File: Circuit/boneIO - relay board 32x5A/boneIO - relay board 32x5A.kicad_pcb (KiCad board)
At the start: 2 copper layers, 197 x 102 mm, 81 parts, among them J1 Screw_Terminal_01x03, J10 Screw_Terminal_01x03, J11 Screw_Terminal_01x03, J12 Conn_02x04_Odd_Even, J13 Screw_Terminal_01x03, J14 Screw_Terminal_01x03, J15 Screw_Terminal_01x03, J16 Screw_Terminal_01x03, J17 Screw_Terminal_01x03, J2 Screw_Terminal_01x03, J3 Screw_Terminal_01x03, J4 Screw_Terminal_01x03, J5 Screw_Terminal_01x03, J6 Screw_Terminal_01x03, J7 Screw_Terminal_01x03, J8 Screw_Terminal_01x03, J9 Screw_Terminal_01x03, K1 HF46F, K10 HF46F, K11 HF46F, K12 HF46F, K13 HF46F, K14 HF46F, K15 HF46F, K16 HF46F, K17 HF46F, K18 HF46F, K19 HF46F, K2 HF46F, K20 HF46F, K21 HF46F, K22 HF46F, K23 HF46F, K24 HF46F, K25 HF46F, K26 HF46F, K27 HF46F, K28 HF46F, K29 HF46F, K3 HF46F, K30 HF46F, K31 HF46F, K32 HF46F, K4 HF46F, K5 HF46F, K6 HF46F, K7 HF46F, K8 HF46F, K9 HF46F, SW1 SW_DIP_x03, SW2 SW_DIP_x03, SW3 SW_DIP_x03, U1 MCP23017_SS, U2 ULN2803A, U3 ULN2803A, U4 MCP23017_SS, U5 ULN2803A, U6 ULN2803A, U7 MCP9808_MSOP

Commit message: relay 32x5 directory cleanup
added shared library with footprints
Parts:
- removed the G*** at (305.4, 311.5)
- added G***: LOGO, boneIO:boneIO_LOGO, F.Cu at (305.4, 311.6)
- J12: footprint ph80ds-21:PinHeader_2x04_P2.54mm_Vertical -> boneIO:PinHeader_2x04_P2.54mm_Vertical
- K1, K10, K11, K12, K13, K14, K15, K16, K17, K18, K19, K2, K20, K21, K22, K23, K24, K25, K26, K27, K28, K29, K3, K30, K31, K32, K4, K5, K6, K7, K8, K9: footprint HF46F:HF46F -> boneIO:HF46F

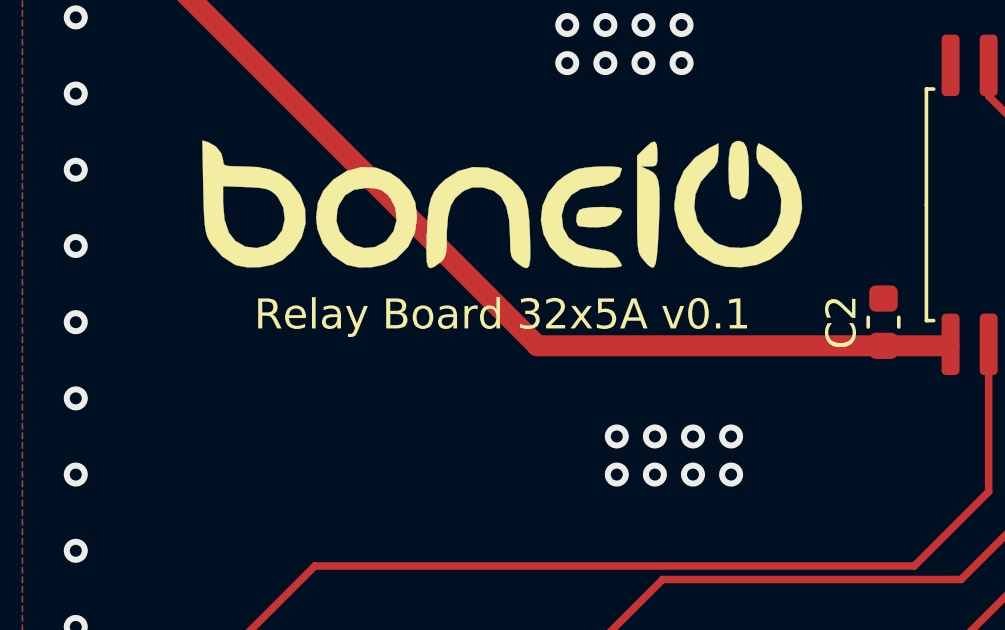
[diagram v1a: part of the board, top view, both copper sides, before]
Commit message: Changed board labels
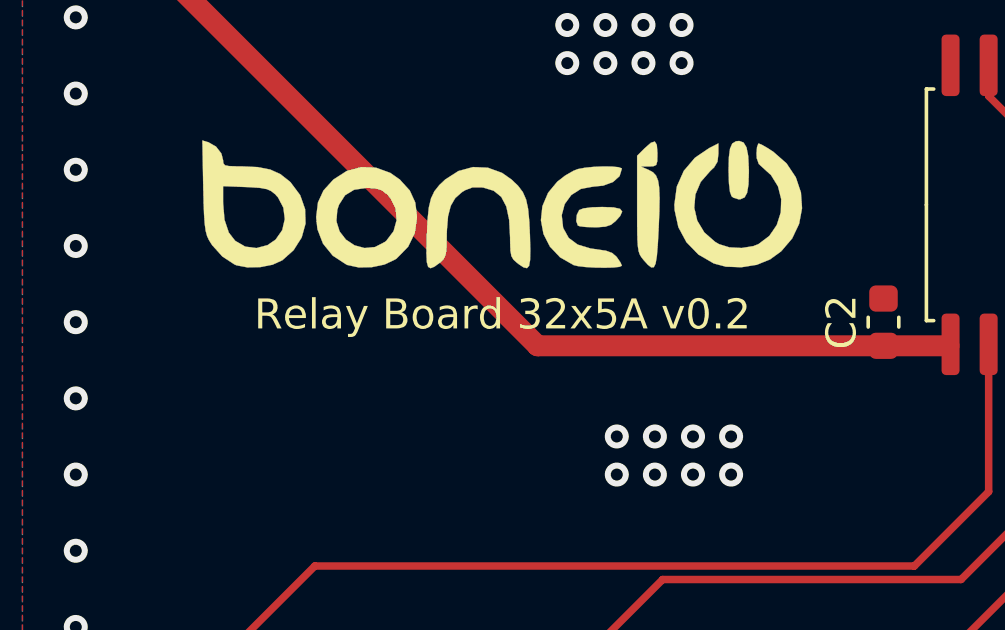
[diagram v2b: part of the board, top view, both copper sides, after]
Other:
- board text added: "Relay Board 32x5A v0.2"
- board text removed: "Relay Board 32x5A v0.1"
